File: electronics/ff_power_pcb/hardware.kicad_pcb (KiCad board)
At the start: 4 copper layers, 50 x 30 mm, 55 parts, among them U3 TPS62095RGTR, U4 TPS62095RGTR, U5 TPS62095RGTR, U6 TPS62095RGTR, U7 AP131-25

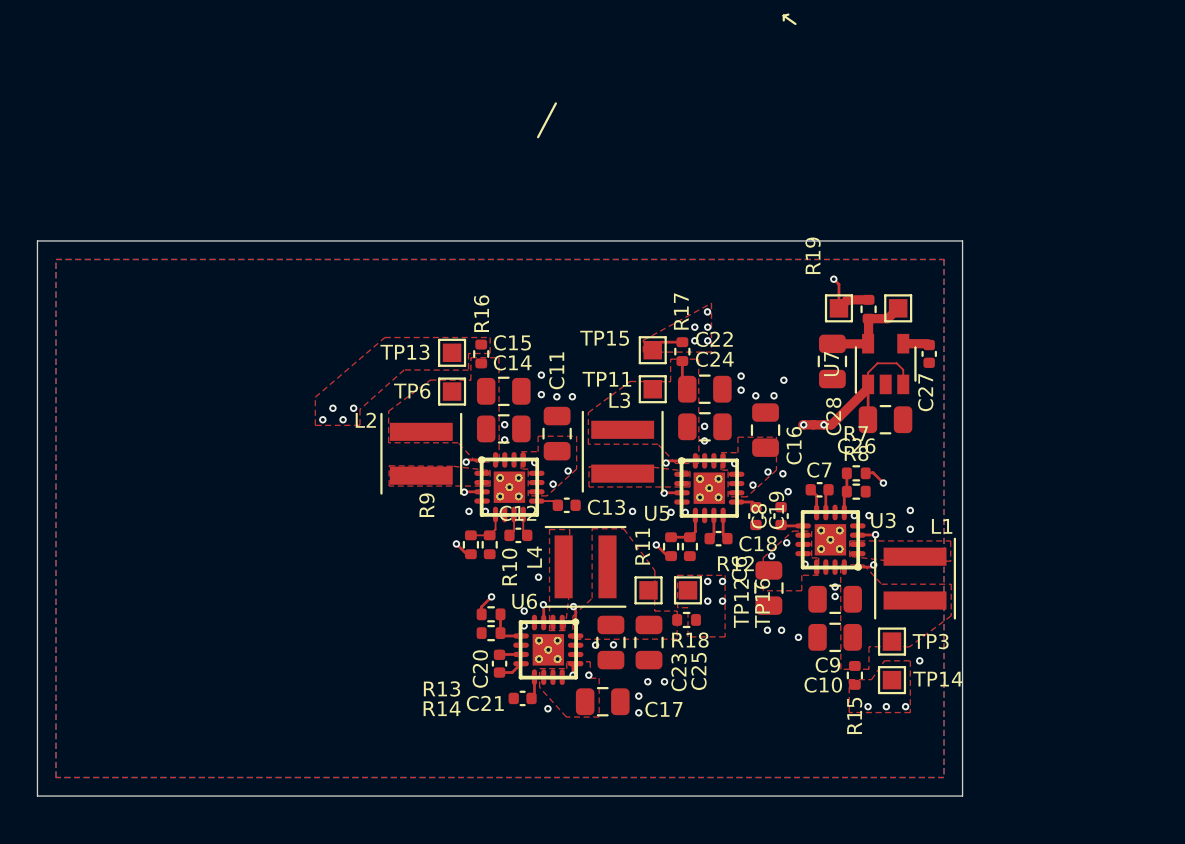
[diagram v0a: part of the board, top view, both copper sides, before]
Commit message: Initial power board in the CAD.
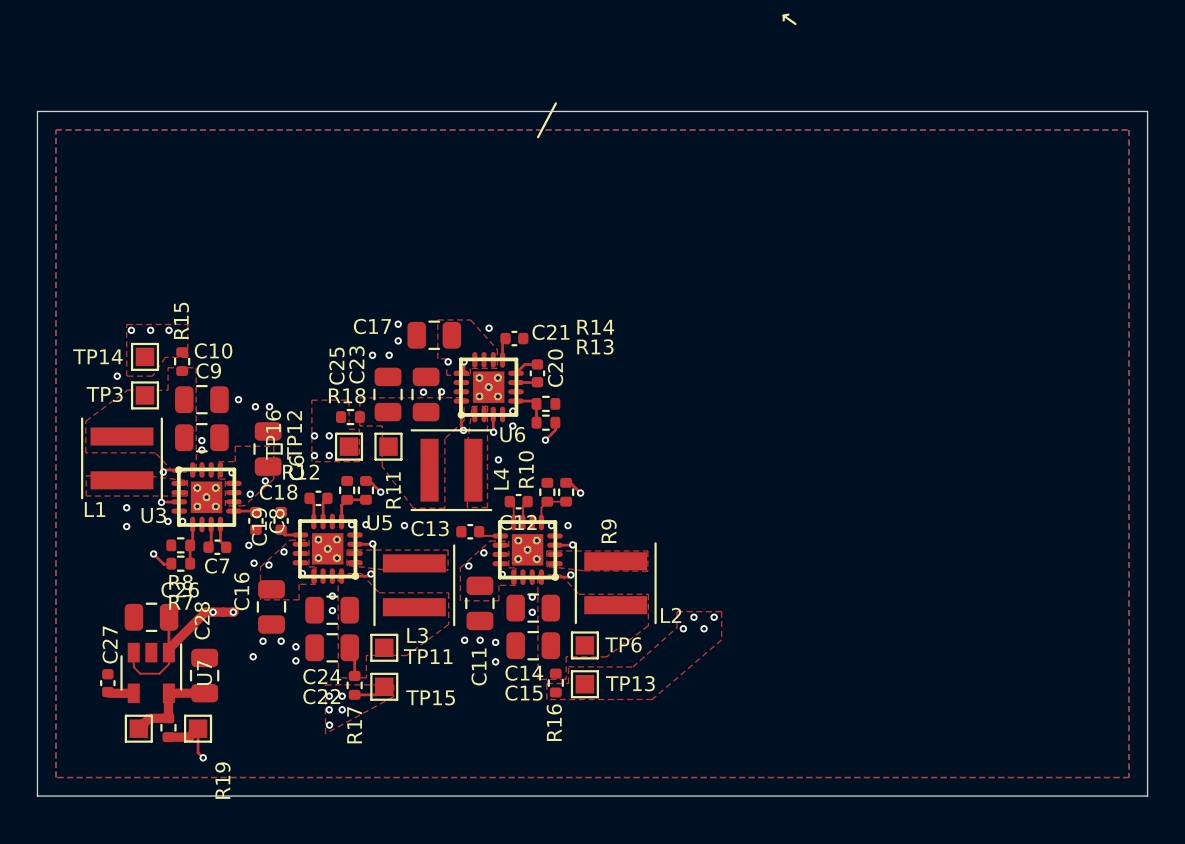
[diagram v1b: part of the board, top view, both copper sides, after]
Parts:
- moved C27 47.8 mm to (103.8, 163.9), turned to 90 degrees
- moved TP17 46.9 mm to (105.5, 166.4), turned to 270 degrees
- moved R19 44.1 mm to (107.1, 166.3), turned to 90 degrees
- moved TP14 44.0 mm to (105.8, 146.3), turned to 0 degrees
- moved L1 43.4 mm to (104.6, 151.8), turned to 90 degrees
- moved U7 43.1 mm to (106.2, 163.3), turned to 270 degrees
- moved TP3 42.5 mm to (105.8, 148.3), turned to 0 degrees
- moved TP18 41.4 mm to (108.7, 166.4), turned to 270 degrees
- moved C26 41.1 mm to (106.2, 160.3), turned to 180 degrees
- moved R15 40.1 mm to (107.8, 146.5), turned to 270 degrees
- moved C28 37.9 mm to (109.0, 163.5), turned to 90 degrees
- moved R7 36.8 mm to (107.7, 157.4), turned to 0 degrees
- moved R8 36.6 mm to (107.7, 156.5), turned to 180 degrees
- moved C10 36.6 mm to (108.9, 148.6), turned to 0 degrees
- moved C9 35.3 mm to (108.9, 150.6), turned to 0 degrees
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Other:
- board size 50 x 30 mm -> 60 x 37 mm

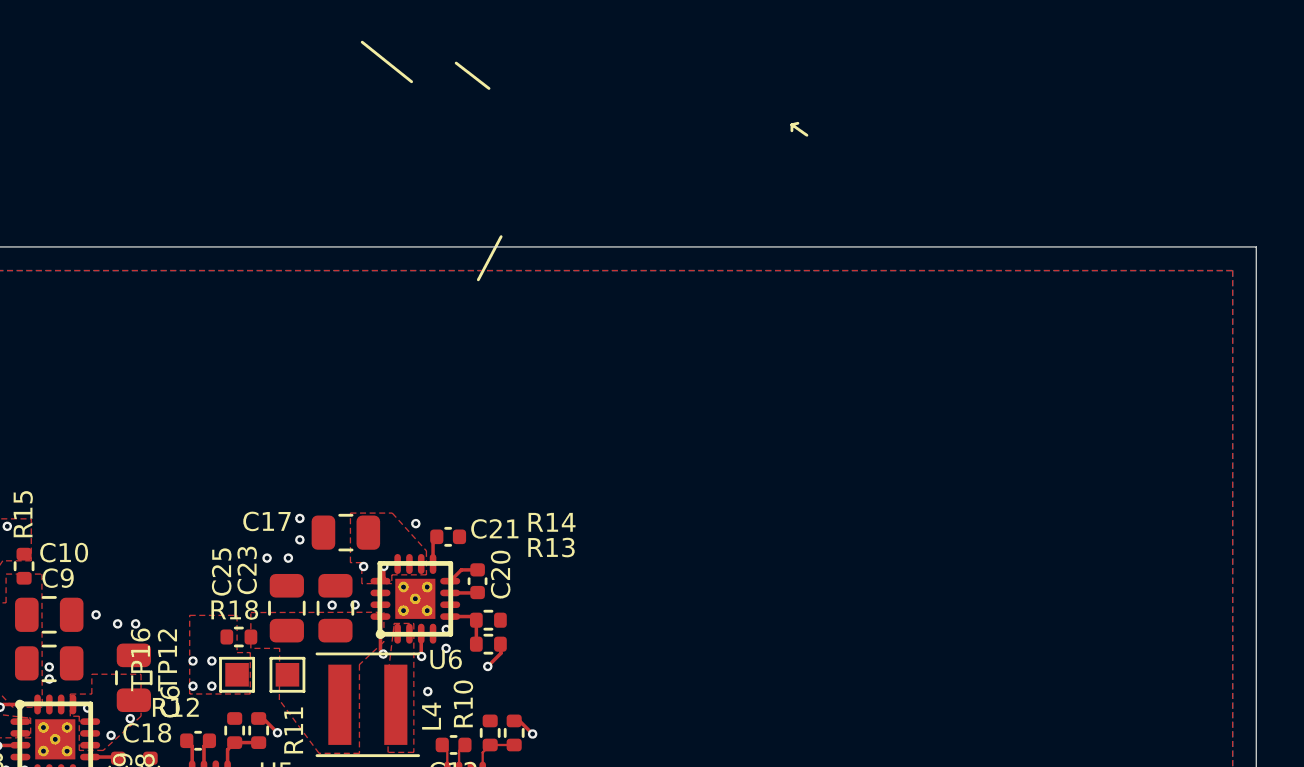
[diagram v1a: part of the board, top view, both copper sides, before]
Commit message: Dopped all the parts down for the power supply.
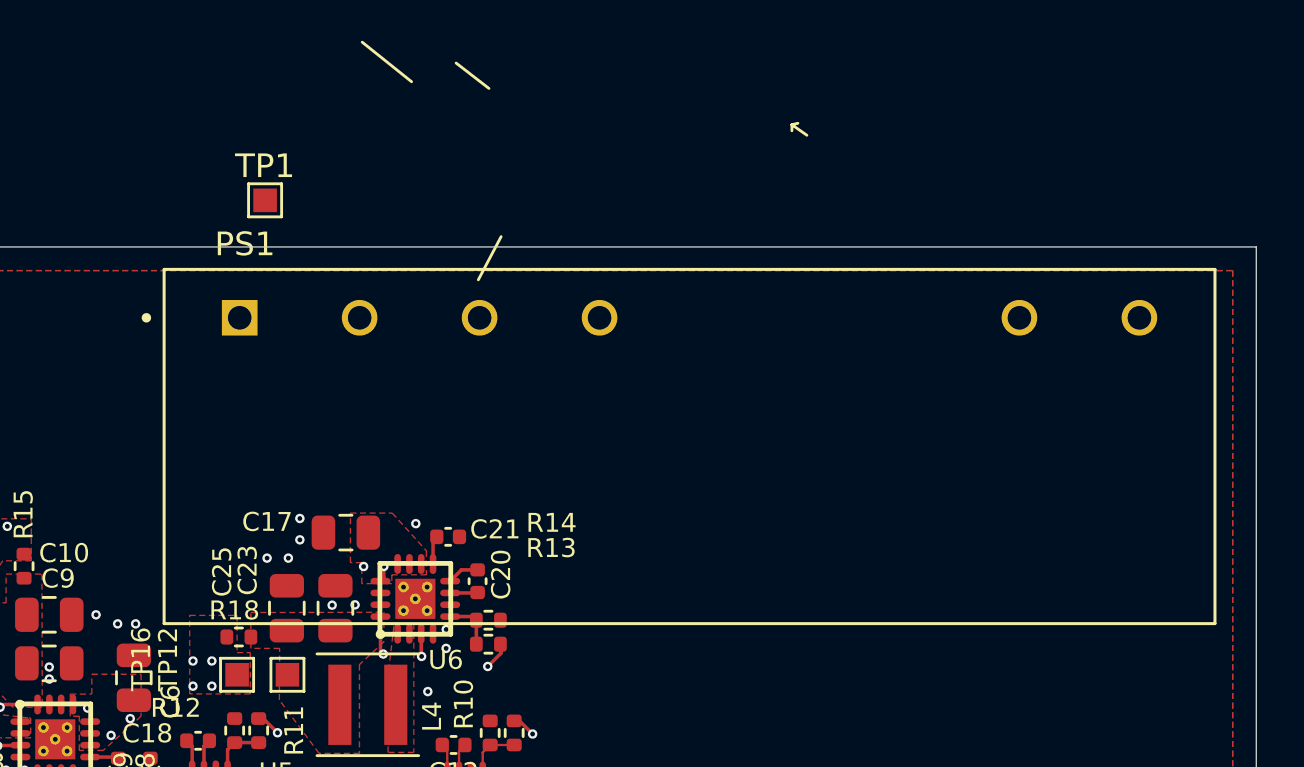
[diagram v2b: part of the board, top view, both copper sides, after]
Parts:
- added PS1: PBO-15C-5, CUI:CONV_PBO-15C-5, F.Cu at (136.0, 136.0)
- added TP1: TestPoint, TestPoint:TestPoint_Pad_1.0x1.0mm, F.Cu at (118.0, 131.0)

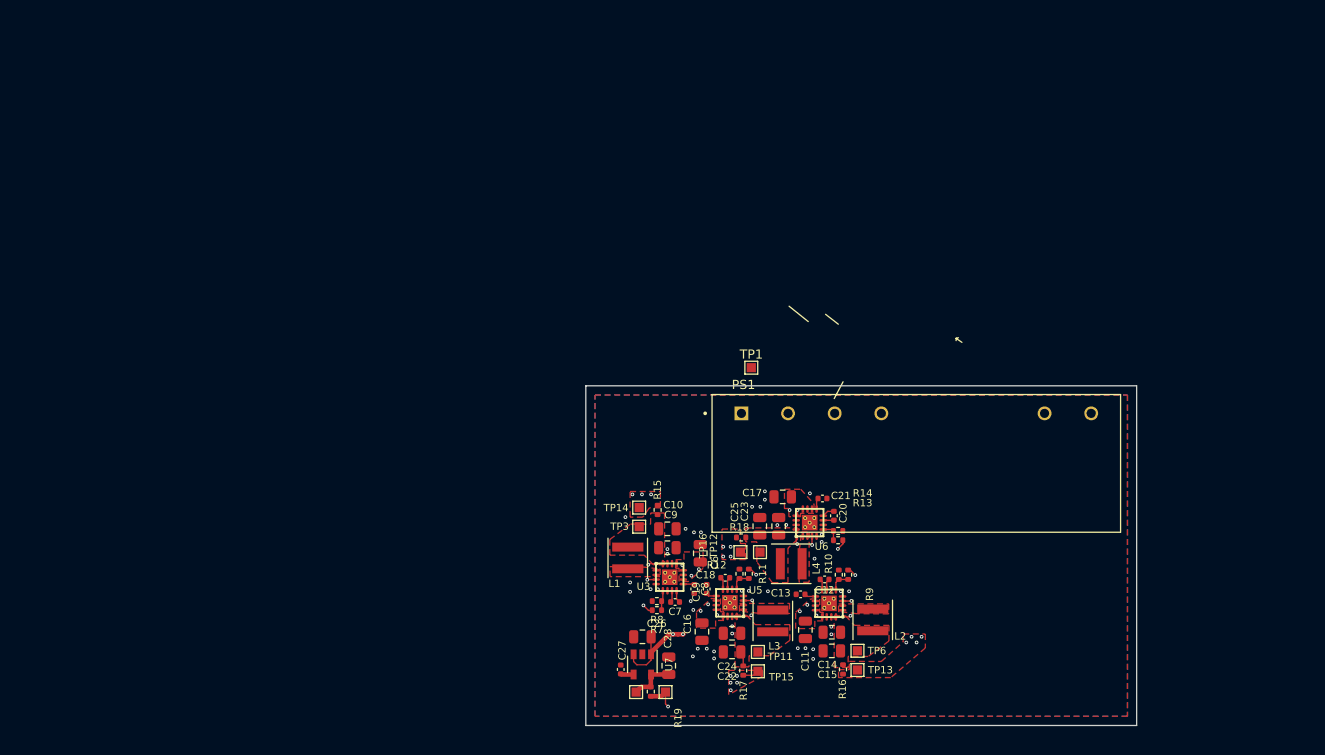
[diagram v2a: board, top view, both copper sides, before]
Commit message: Dropping the parts into the layout.
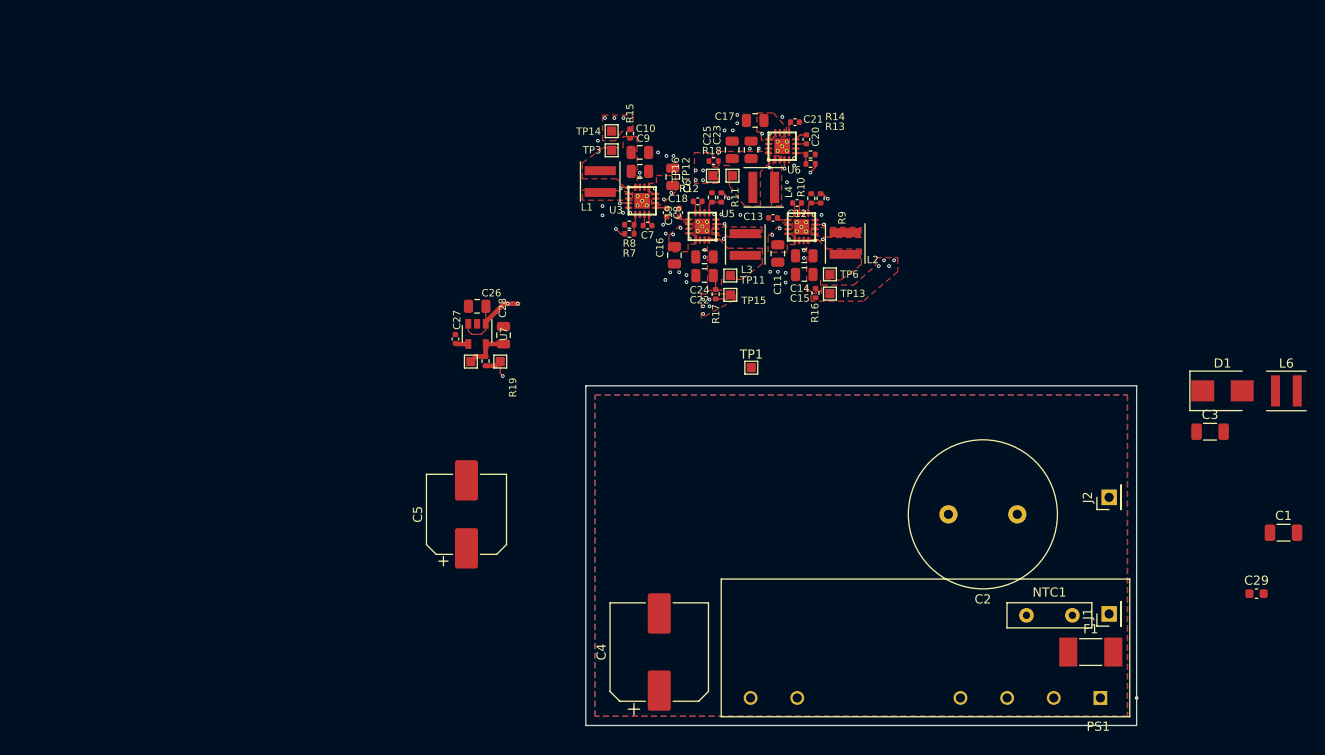
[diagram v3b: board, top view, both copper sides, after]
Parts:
- added C1: 0.1uF, Capacitor_SMD:C_1206_3216Metric, F.Cu at (176.0, 149.0)
- added C2: 33uF, Capacitor_THT:C_Radial_D16.0mm_H25.0mm_P7.50mm, F.Cu at (147.0, 147.0)
- added C29: 0.1uF, Capacitor_SMD:C_0603_1608Metric, F.Cu at (173.1, 155.6)
- added C3: 2.2nF, Capacitor_SMD:C_1206_3216Metric, F.Cu at (168.0, 138.0)
- added C4: 470uF, Capacitor_SMD:CP_Elec_10x12.5, F.Cu at (108.0, 162.0)
- added C5: 220uF, Capacitor_SMD:CP_Elec_8x10.5, F.Cu at (87.0, 147.0)
- added D1: SMBJ7.0A, Diode_SMD:D_SMB, F.Cu at (169.3, 133.6)
- added F1: 1A/300V Slow, Fuse:Fuse_Littelfuse-NANO2-451_453, F.Cu at (155.0, 162.0)
- added J1: Conn_01x01_Female, Connector_PinHeader_2.54mm:PinHeader_1x01_P2.54mm_Vertical, F.Cu at (157.0, 157.8)
- added J2: Conn_01x01_Female, Connector_PinHeader_2.54mm:PinHeader_1x01_P2.54mm_Vertical, F.Cu at (157.0, 145.2)
- added L6: 2.2uH, Inductor_SMD:L_Coilcraft_XxL4020, F.Cu at (176.3, 133.6)
- added NTC1: 10R, Capacitor_THT:C_Disc_D9.0mm_W2.5mm_P5.00mm, F.Cu at (148.0, 158.0)
- moved C16 41.1 mm to (109.6, 118.8)
- moved C18 41.1 mm to (112.2, 112.9)
- moved C19 41.1 mm to (110.2, 114.1)
- moved C21 41.1 mm to (122.8, 104.3)
- moved C22 41.1 mm to (112.9, 121.0)
- moved C8 41.1 mm to (108.8, 114.1)
- moved R16 41.1 mm to (125.0, 122.9)
- moved TP11 41.1 mm to (115.7, 121.0)
- moved TP14 41.1 mm to (102.8, 105.3)
- moved U3 41.1 mm to (106.1, 112.8)
- moved C10 41.1 mm to (105.9, 107.6)
- moved C11 41.1 mm to (120.9, 118.6)
- moved C12 41.1 mm to (123.0, 113.1)
- moved C15 41.1 mm to (123.8, 120.9)
- moved C20 41.1 mm to (124.0, 106.2)
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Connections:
- PS1 pad 1: (no net) -> /AC_N
- PS1 pad 14: (no net) -> GND
- PS1 pad 16: (no net) -> Net-(C4-Pad1)
- PS1 pad 5: (no net) -> Net-(C2-Pad1)
- PS1 pad 7: (no net) -> Net-(C2-Pad2)

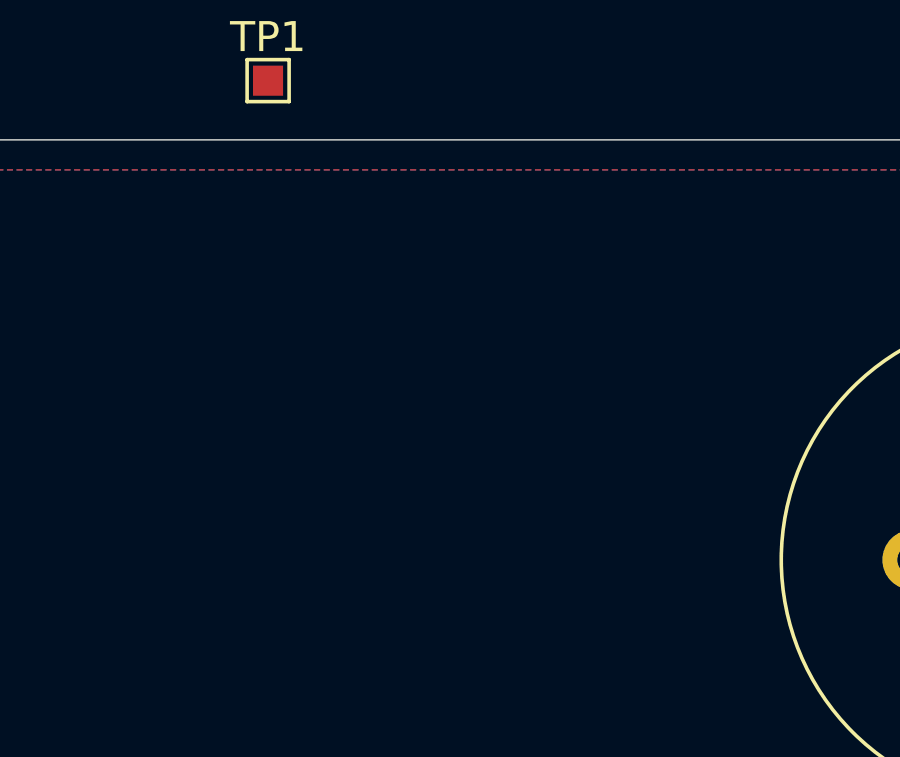
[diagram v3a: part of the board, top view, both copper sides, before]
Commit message: All footprints are in.
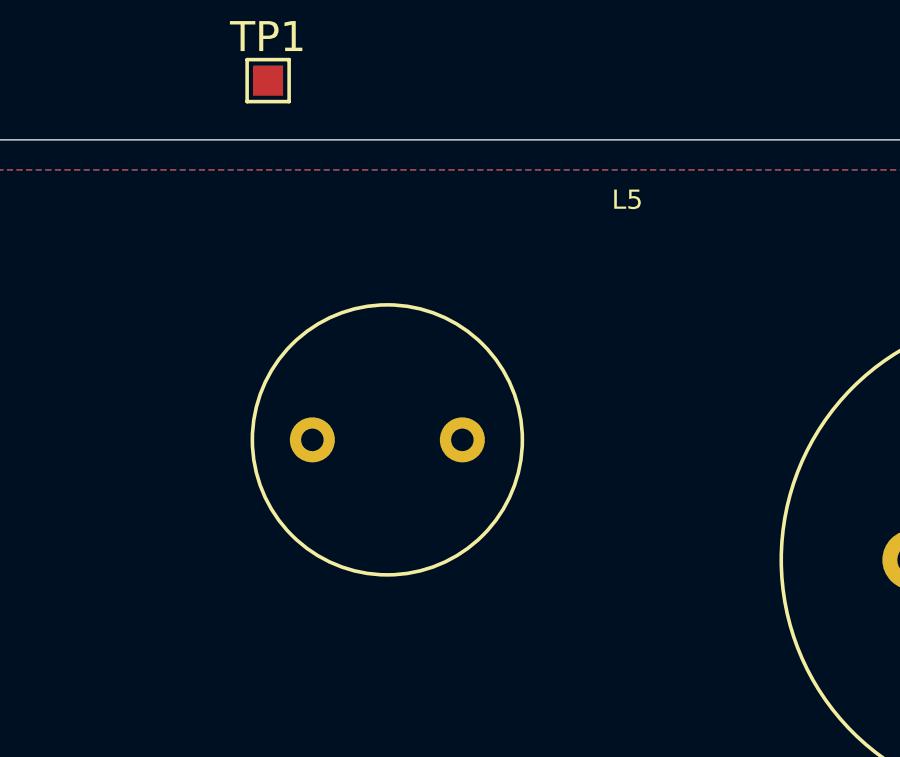
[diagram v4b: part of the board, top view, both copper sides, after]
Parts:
- added L5: 1.2mH, Bourns:RLB9012, F.Cu at (122.0, 143.0)
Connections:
- PS1 pad 3: (no net) -> Net-(L5-Pad2)
